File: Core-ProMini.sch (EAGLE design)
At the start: 94 parts, among them J1 RJ12, J3 CONNECTOR-GROVE-4P-2.0-347013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, J4 CONNECTOR-DC-POWER-RA, J8 RJ12, Q1 2N3904, Q10 MOSFET-P-044021001, Q11 MOSFET-P-044021001, Q12 MOSFET-P-044021001, Q13 MOSFET-P-044021001, Q4 MOSFET-P mouser 78-SI2347DS-T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, Q5 MOSFET-P-044021001, Q6 MOSFET-P-044021001, Q7 MOSFET-P-044021001, Q8 MOSFET-P-044021001, Q9 MOSFET-P-044021001, U1 LM393M, U2 LM317

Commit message: removed loconet interface
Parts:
- removed B1: DBDB101G, rectifier:DBDB101G
- removed J1, J8: RJ12, SPCoast:CONNECTOR-RJ25CORCOM
- removed J3: CONNECTOR-GROVE-4P-2.0-3470130P1, SPCoast:CONNECTOR-GROVE-4P-2.0-3470130P1
- removed JP1: LN-TERM, MCP:JUMPER-2PTH_LOCK
- removed JP5: I2C Power, SparkFun-Connectors:M02LOCK
- removed LED1: Blue, SPCoast:LED0805-LED
- removed LED10, LED11, LED12, LED13, LED4, LED5, LED6, LED7, LED8, LED9, LEDA0, LEDA1, LEDA2, LEDA3, LEDA4, LEDA5: Y-0330050P1, SPCoast:LED0603-LED
- removed Q1: 2N3904, MCP:NPN-SOT23-3
- removed Q10, Q11, Q12, Q13, Q5, Q6, Q7, Q8, Q9, QA0, QA1, QA2, QA3, QA4, QA5: MOSFET-P-044021001, SPCoast:MOSFET-P-044021001
- removed Q4: MOSFET-P mouser 78-SI2347DS-T1-GE3 30V .042Ohm@10V 5A P-Ch 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, SPCoast:MOSFET-P-044021001
- removed R1: 4k7, SPCoast:R0805-RES
- removed R10, R11, R12, R13, R4, R5, R6, R7, R8, R9, RA0, RA1, RA2, RA3, RA4, RA5: 2K2, SPCoast:R0805-RES
- removed R14: 39k, SPCoast:R0805-RES
- removed R15: 27k, SPCoast:R0805-RES
- removed R16: 240k, SPCoast:R0805-RES
- removed R17: 1k, SPCoast:R0805-RES
- removed R18: 470R, SPCoast:R0805-RES
- removed R19: 47R, SPCoast:R0805-RES
- removed R2: 150k, SPCoast:R0805-RES
- removed R20: 82R, SPCoast:R0805-RES
- removed R3: 47k, SPCoast:R0805-RES
- removed RA6, RA7: 10k, SPCoast:R0805-RES
- removed S1: DPDT, SPCoast:SWITCH-DPDTAYZ0202
- removed U1: LM393M, MCP:LM393M
- removed U2: LM317, MCP:LM317LD
- added CON1: (no value), SPCoast:CONNECTOR-M02508-LOCK
- added I2C-POWER: (no value), SPCoast:JUMPER-2PTH_LOCK
- C5: device SPCoast:CAP-POL0810 -> SPCoast:CAP-POLPTH-5MM
- J4: value CONNECTOR-DC-POWER-RA -> (none)
- JP10, JP11, JP12, JP13: device SparkFun-Connectors:M06LOCK -> SPCoast:CONNECTOR-M06LOCK
- R111: value 1k8 -> 2k-5k
- U$4: value BOARD80X100 -> BOARD69X100MRCS; device SPCoast:BOARD80X100 -> SPCoast:BOARD69X100MRCS
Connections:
- removed net LNRX: LED1.C, R16.2, R17.2, U$2.D8, U1G2.OUT
- removed net LNTX: R1.1, U$2.D7
- removed net LOCONET: J1.3, J1.4, J8.3, J8.4, JP1.1, Q1.C, R3.1
- removed net N$1: Q1.B, R1.2
- removed net N$10: LED6.A, R6.1
- removed net N$11: Q1.E, R19.1
- removed net N$12: Q5.D, R5.2
- removed net N$13: Q6.D, R6.2
- removed net N$14: Q7.D, R7.2
- removed net N$15: LED7.A, R7.1
- removed net N$16: LED11.A, R11.1
- removed net N$17: LED10.A, R10.1
- removed net N$18: LED9.A, R9.1
- removed net N$19: Q8.D, R8.2
- removed net N$20: Q9.D, R9.2
- removed net N$21: Q10.D, R10.2
- removed net N$22: Q11.D, R11.2
- removed net N$23: LED8.A, R8.1
- removed net N$24: LED12.A, R12.1
- removed net N$25: LED13.A, R13.1
- removed net N$26: LEDA0.A, RA0.1
- removed net N$27: Q12.D, R12.2
- removed net N$28: LEDA1.A, RA1.1
- removed net N$29: Q13.D, R13.2
- removed net N$30: JP1.2, R20.2, U2.ADJ
- removed net N$31: B1.AC1, S1.1A
- removed net N$32: B1.AC2, S1.2A
- removed net N$33: QA0.D, RA0.2
- removed net N$34: QA1.D, RA1.2
- removed net N$35: LEDA5.A, RA5.1
- removed net N$36: LEDA4.A, RA4.1
- removed net N$37: LEDA3.A, RA3.1
- removed net N$38: LEDA2.A, RA2.1
- removed net N$39: QA2.D, RA2.2
- removed net N$4: R16.1, R2.2, R3.2, U1G2.+IN
- removed net N$40: QA3.D, RA3.2
- removed net N$41: QA4.D, RA4.2
- removed net N$42: QA5.D, RA5.2
- removed net N$5: R14.2, R15.2, U1G2.-IN
- removed net N$6: LED1.A, R18.2
- removed net N$7: LED4.A, R4.1
- removed net N$8: Q4.D, R4.2
- removed net N$9: LED5.A, R5.1
- removed net RAILSYNC-A: J1.6, J8.6, S1.1C
- removed net RAILSYNC-B: J1.1, J8.1, S1.2C
- removed net VOUT: R20.1, U2.VO, U2.VO@1, U2.VO@2, U2.VO@3
- new net D7: J5.3, JP11.3, U$2.D7
- new net D8: J5.4, JP11.4, U$2.D8
- net +9V: now also CON1.A; no longer B1.+, J3.3, J3.4, U2.VI
- net A0: now also J7.2, JP13.2; no longer J6.4, JP12.4, QA0.G
- net A1: now also J7.3, JP13.3; no longer J6.5, JP12.5, QA1.G
- net A2: now also J7.4, JP13.4; no longer J7.2, JP13.2, QA2.G
- net A3: now also J7.5, JP13.5; no longer J7.3, JP13.3, QA3.G
- net A6: no longer J7.4, JP13.4, QA4.G, RA6.1
- net A7: no longer J7.5, JP13.5, QA5.G, RA7.1
- net D10: now also J6.2, JP12.2; no longer J5.4, JP11.4, Q10.G
- net D11: now also J6.3, JP12.3; no longer J5.5, JP11.5, Q11.G
- net D12: now also J6.4, JP12.4; no longer J6.2, JP12.2, Q12.G
- net D13: now also J6.5, JP12.5; no longer J6.3, JP12.3, Q13.G
- net D2: no longer Q4.G
- net D3: no longer Q5.G
- net D4: no longer Q6.G
- net D5: no longer Q7.G
- net D6: no longer Q8.G
- net D9: now also J5.5, JP11.5; no longer J5.3, JP11.3, Q9.G
- net GND: now also CON1.B; no longer B1.-, J1.2, J1.5, J3.1, J3.2, J8.2, J8.5, LED10.C, LED11.C, LED12.C, LED13.C, LED4.C, LED5.C, LED6.C, LED7.C, LED8.C, LED9.C, LEDA0.C, LEDA1.C, LEDA2.C, LEDA3.C, LEDA4.C, LEDA5.C, R14.1, R19.2, R2.1, U1G1.+IN, U1G1.-IN, U1G1.V-
- net N$44: now also I2C-POWER.1; no longer JP5.1
- net VCCIO: now also I2C-POWER.2; no longer JP5.2, Q10.S, Q11.S, Q12.S, Q13.S, Q4.S, Q5.S, Q6.S, Q7.S, Q8.S, Q9.S, QA0.S, QA1.S, QA2.S, QA3.S, QA4.S, QA5.S, R15.1, R17.1, R18.1, RA6.2, RA7.2, U1G1.V+
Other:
- note removed: "1.5"
- note removed: "Added Railsync VIN power"
- note removed: "Loconet Interface"
- note removed: "Loconet Shield"
- note removed: "Note: Added RailSync power source connection to VIN to remotely power 'duino"

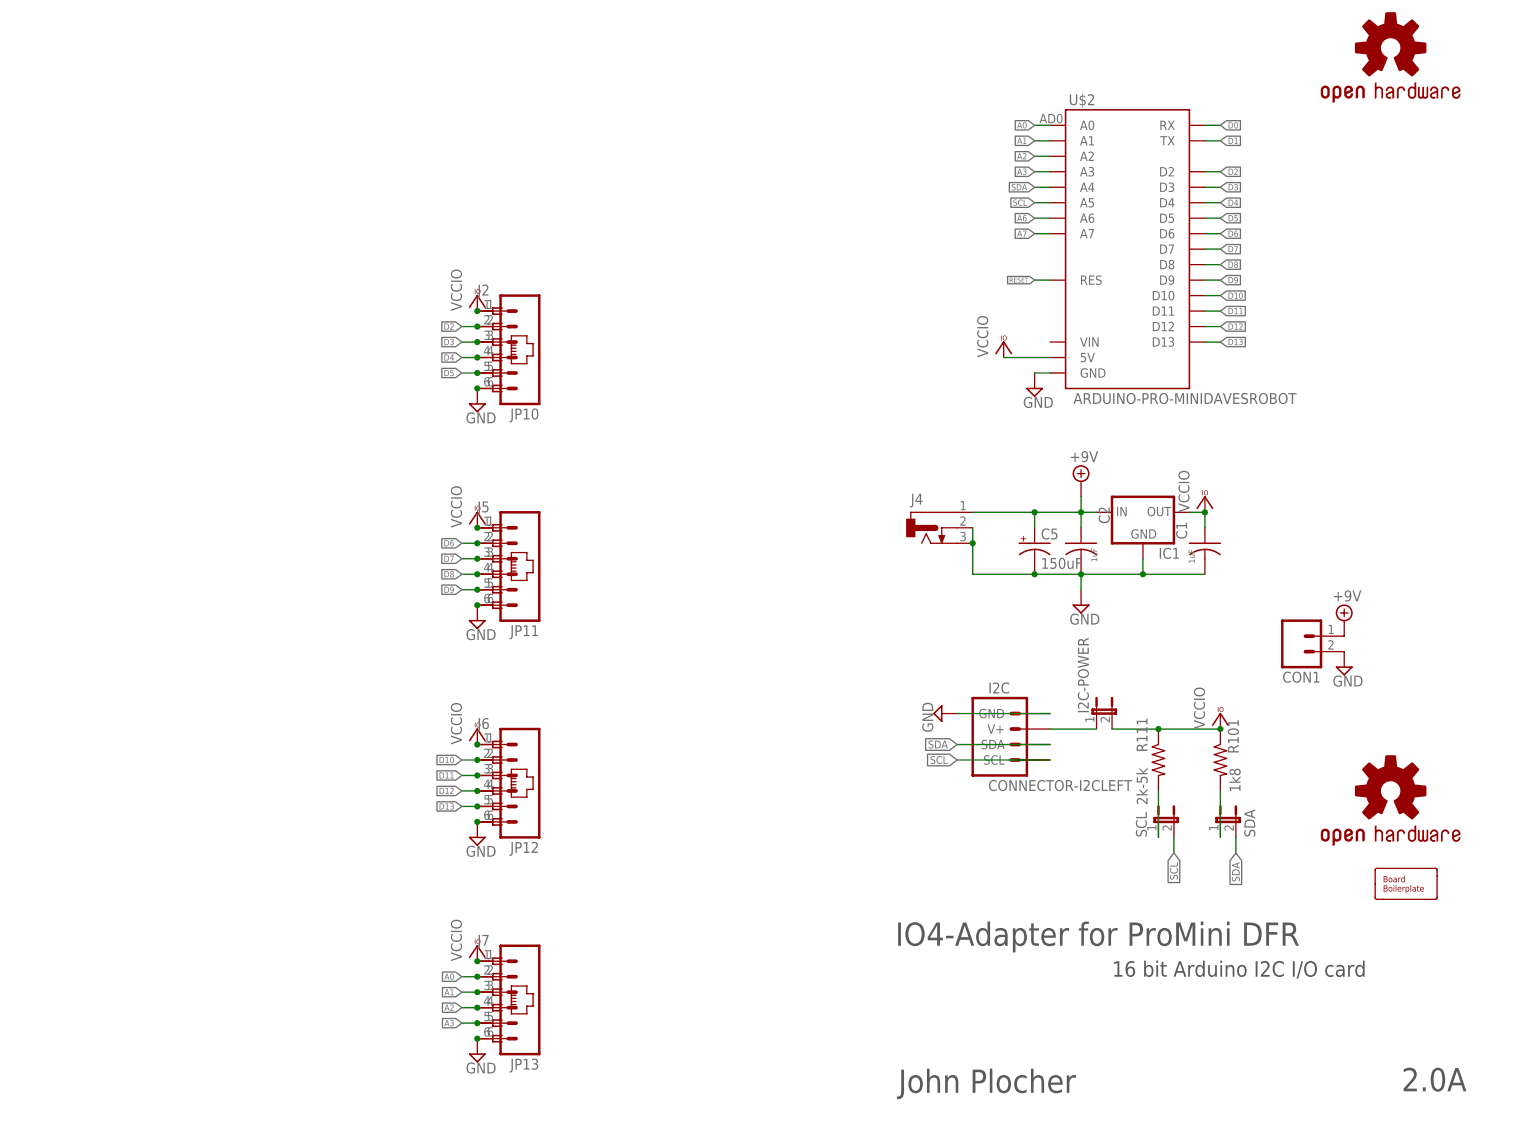
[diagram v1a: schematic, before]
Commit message: updated part values and silkscreen, added cmri-io
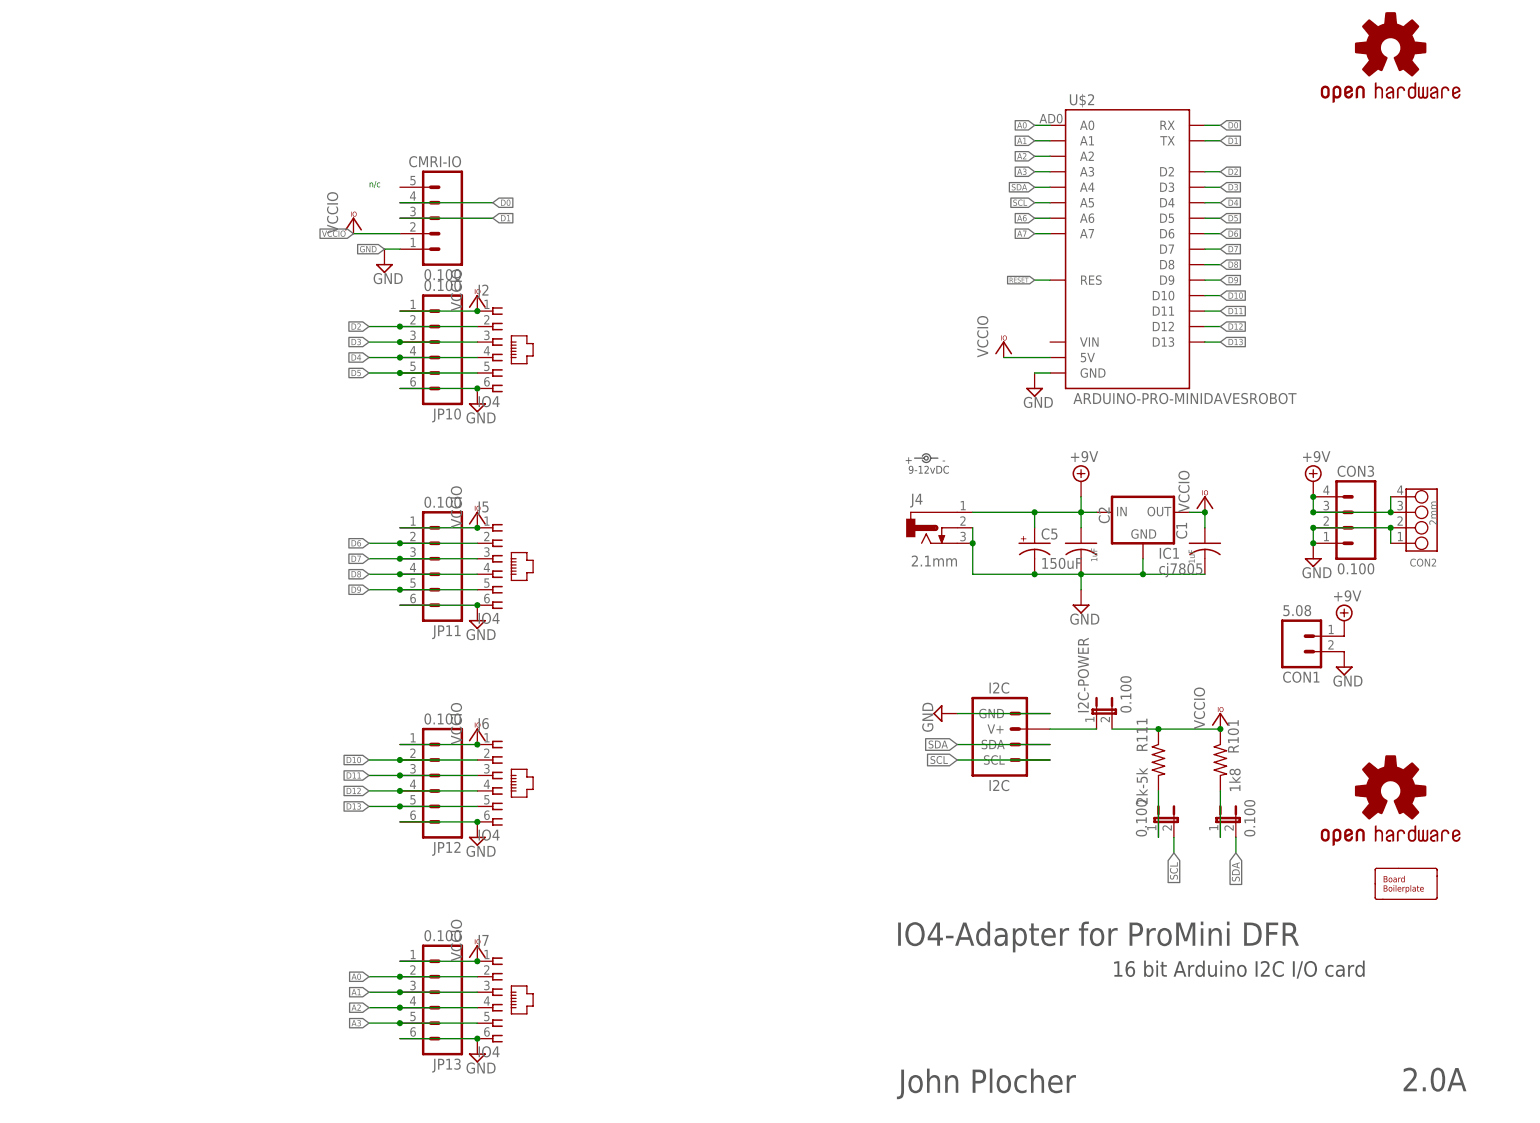
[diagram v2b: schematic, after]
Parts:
- added CMRI-IO: 0.100, SPCoast:CONNECTOR-M05CMRI
- added CON2: 2mm, SPCoast:CONNECTOR-GROVE-4P-2.0-3470130P1
- added CON3: 0.100, SPCoast:CONNECTOR-M04LOCK
- C5: device SPCoast:CAP-POLPTH-5MM -> SPCoast:CAP-POL0810
- CON1: value (none) -> 5.08
- I2C: value CONNECTOR-I2CLEFT -> I2C
- I2C-POWER, JP10, JP11, JP12, JP13: value (none) -> 0.100
- IC1: value (none) -> cj7805; device SPCoast:VREG_78XX-1300040P1 -> SPCoast:VREG-DPAK-5
- J2, J5, J6, J7: value (none) -> IO4; device SPCoast:RJ12CORCOM -> SPCoast:CONNECTOR-RJ25-6P6C
- J4: value (none) -> 2.1mm
- LOGO1: value DOC-OSHW-LOGOL -> DOC-OSHW-LOGO-L; device SPCoast:DOC-OSHW-LOGOL -> SPCoast:DOC-OSHW-LOGO-L
- R101, R111: device SPCoast:RPTH-1/6W -> SPCoast:R0805-RES
- SCL: value SCL -> 0.100
- SDA: value SDA -> 0.100
- U$3: device SPCoast-minimal:POWER_LABEL -> SPCoast:DOC-POWER_LABEL
- renumbered JP2 to SDA, JP3 to SCL
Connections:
- net +9V: now also CON2.3, CON2.4, CON3.3, CON3.4
- net D0: now also CMRI-IO.4
- net D1: now also CMRI-IO.3
- net GND: now also CMRI-IO.1, CON2.1, CON2.2, CON3.1, CON3.2
- net VCCIO: now also CMRI-IO.2
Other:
- note added: "Note: changed I2C pullup to SMT and added CMRI-IO"
- note added: "n/c"
- note removed: "Note: Added pullups to A6, A7 Analog inputs"
- moved on the sheet: JP10, JP11, JP12, JP13
